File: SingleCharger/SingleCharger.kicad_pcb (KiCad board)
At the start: 2 copper layers, 120 x 130 mm, 77 parts, among them J1 Bus_PCI_Express_x1, J2 Conn_01x03_Pin, J3 Conn_01x02_Pin, J4 Conn_01x02_Pin, Q2 TPHR8504PL,LQ(M1W, U1 ADS1115IDGSR, U10 LM358, U11 MCP4725A0T-E/CH, U2 PICO, U3 TPS54360BDDAR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

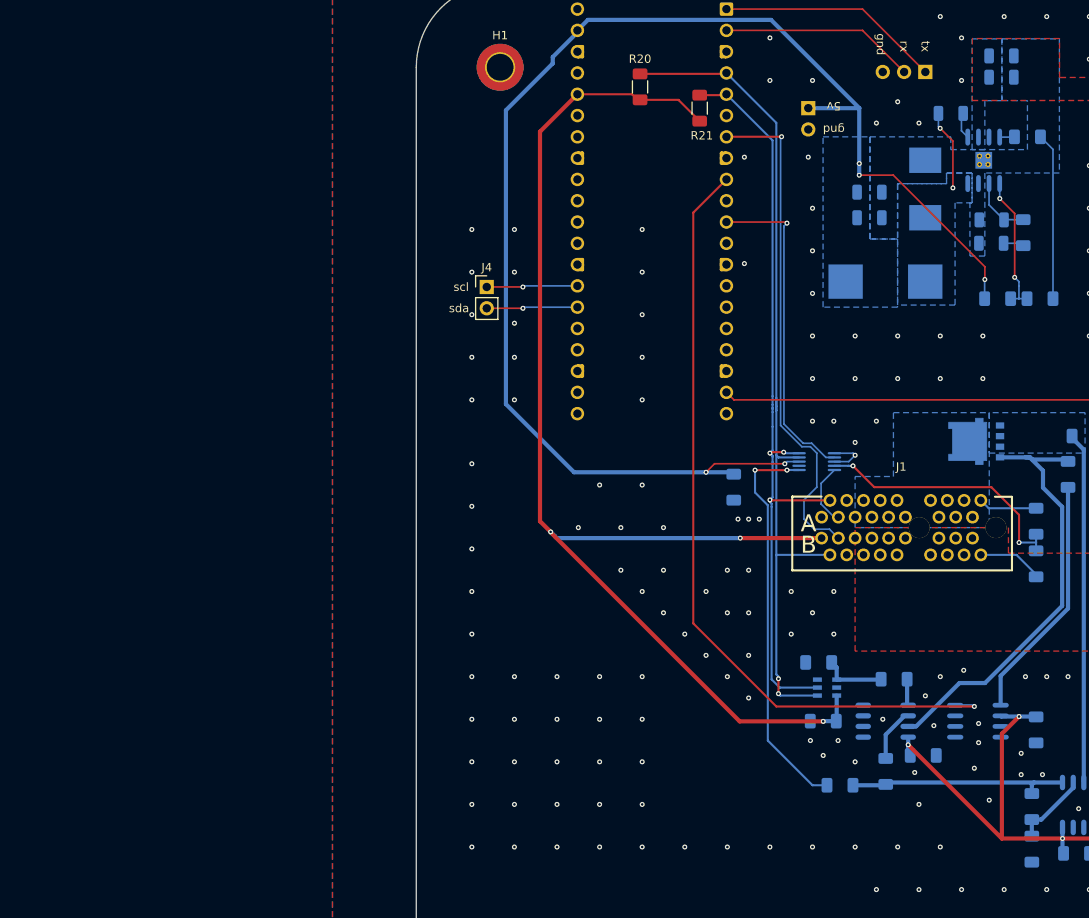
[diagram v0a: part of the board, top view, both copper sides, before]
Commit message: Started adding LEDS
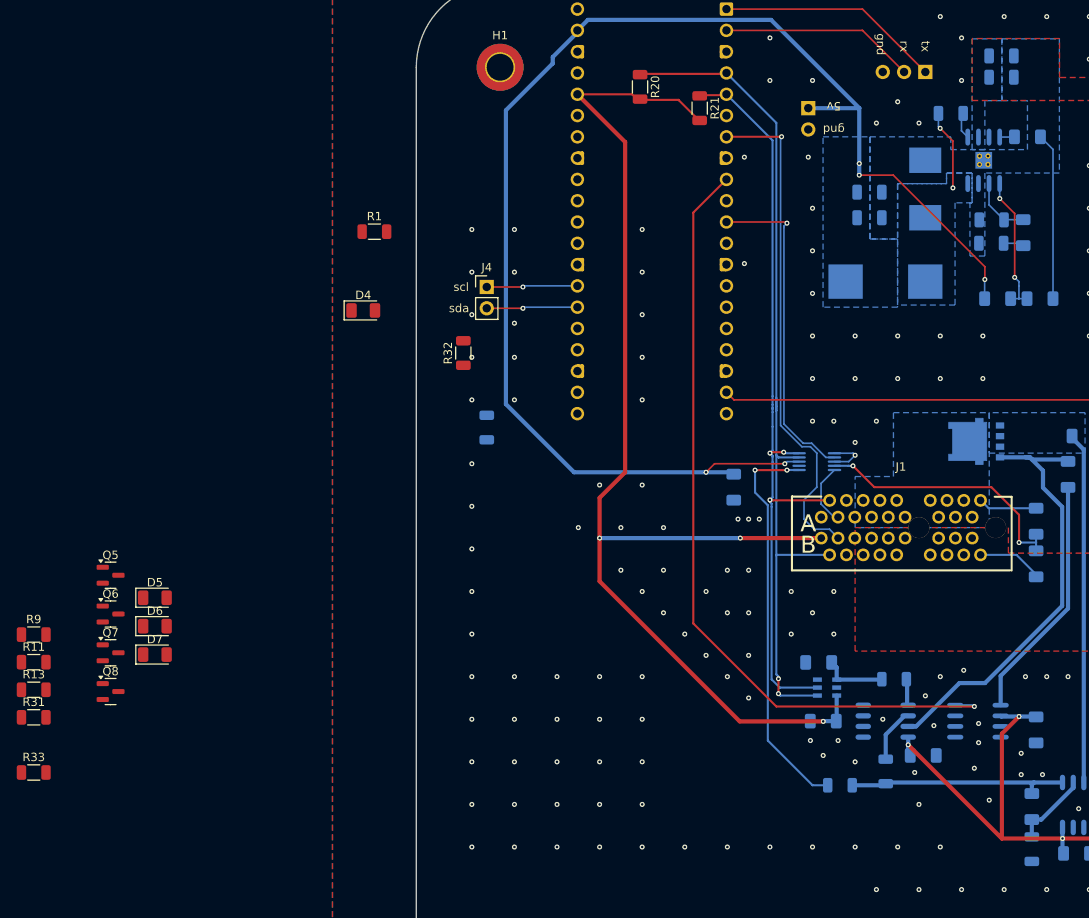
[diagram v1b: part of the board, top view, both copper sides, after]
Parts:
- added D4: LED, LED_SMD:LED_1206_3216Metric, F.Cu at (58.7, 64.0)
- added D5: LED, LED_SMD:LED_1206_3216Metric, F.Cu at (33.8, 98.3)
- added D6: LED, LED_SMD:LED_1206_3216Metric, F.Cu at (33.8, 101.7)
- added D7: LED, LED_SMD:LED_1206_3216Metric, F.Cu at (33.8, 105.1)
- added Q5: NMOS, Package_TO_SOT_SMD:SOT-23, F.Cu at (28.5, 95.6)
- added Q6: NMOS, Package_TO_SOT_SMD:SOT-23, F.Cu at (28.5, 100.2)
- added Q7: NMOS, Package_TO_SOT_SMD:SOT-23, F.Cu at (28.5, 104.8)
- added Q8: NMOS, Package_TO_SOT_SMD:SOT-23, F.Cu at (28.5, 109.5)
- added R1: 1k, Resistor_SMD:R_1206_3216Metric, F.Cu at (60.0, 54.6)
- added R11: 1k, Resistor_SMD:R_1206_3216Metric, F.Cu at (19.4, 106.0)
- added R13: 1k, Resistor_SMD:R_1206_3216Metric, F.Cu at (19.4, 109.3)
- added R31: 1k, Resistor_SMD:R_1206_3216Metric, F.Cu at (19.4, 112.5)
- added R32: 1k, Resistor_SMD:R_1206_3216Metric, F.Cu at (70.6, 69.1)
- added R33: 1k, Resistor_SMD:R_1206_3216Metric, F.Cu at (19.4, 119.1)
- added R5: 1k, Resistor_SMD:R_1206_3216Metric, B.Cu at (73.4, 78.0)
- added R9: 1k, Resistor_SMD:R_1206_3216Metric, F.Cu at (19.4, 102.7)
- R14, R20, R21, R22, R23, R25: footprint Resistor_SMD:R_1206_3216Metric_Pad1.30x1.75mm_HandSolder -> Resistor_SMD:R_1206_3216Metric
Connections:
- U2 pad 21: unconnected-(U2-GP16-Pad21) -> Net-(U2-GP16)
- U2 pad 22: unconnected-(U2-GP17-Pad22) -> Net-(U2-GP17)
- U2 pad 24: unconnected-(U2-GP18-Pad24) -> Net-(U2-GP18)
- U2 pad 25: unconnected-(U2-GP19-Pad25) -> Net-(U2-GP19)
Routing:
- net +3V3: track 149.7 -> 142.4 mm

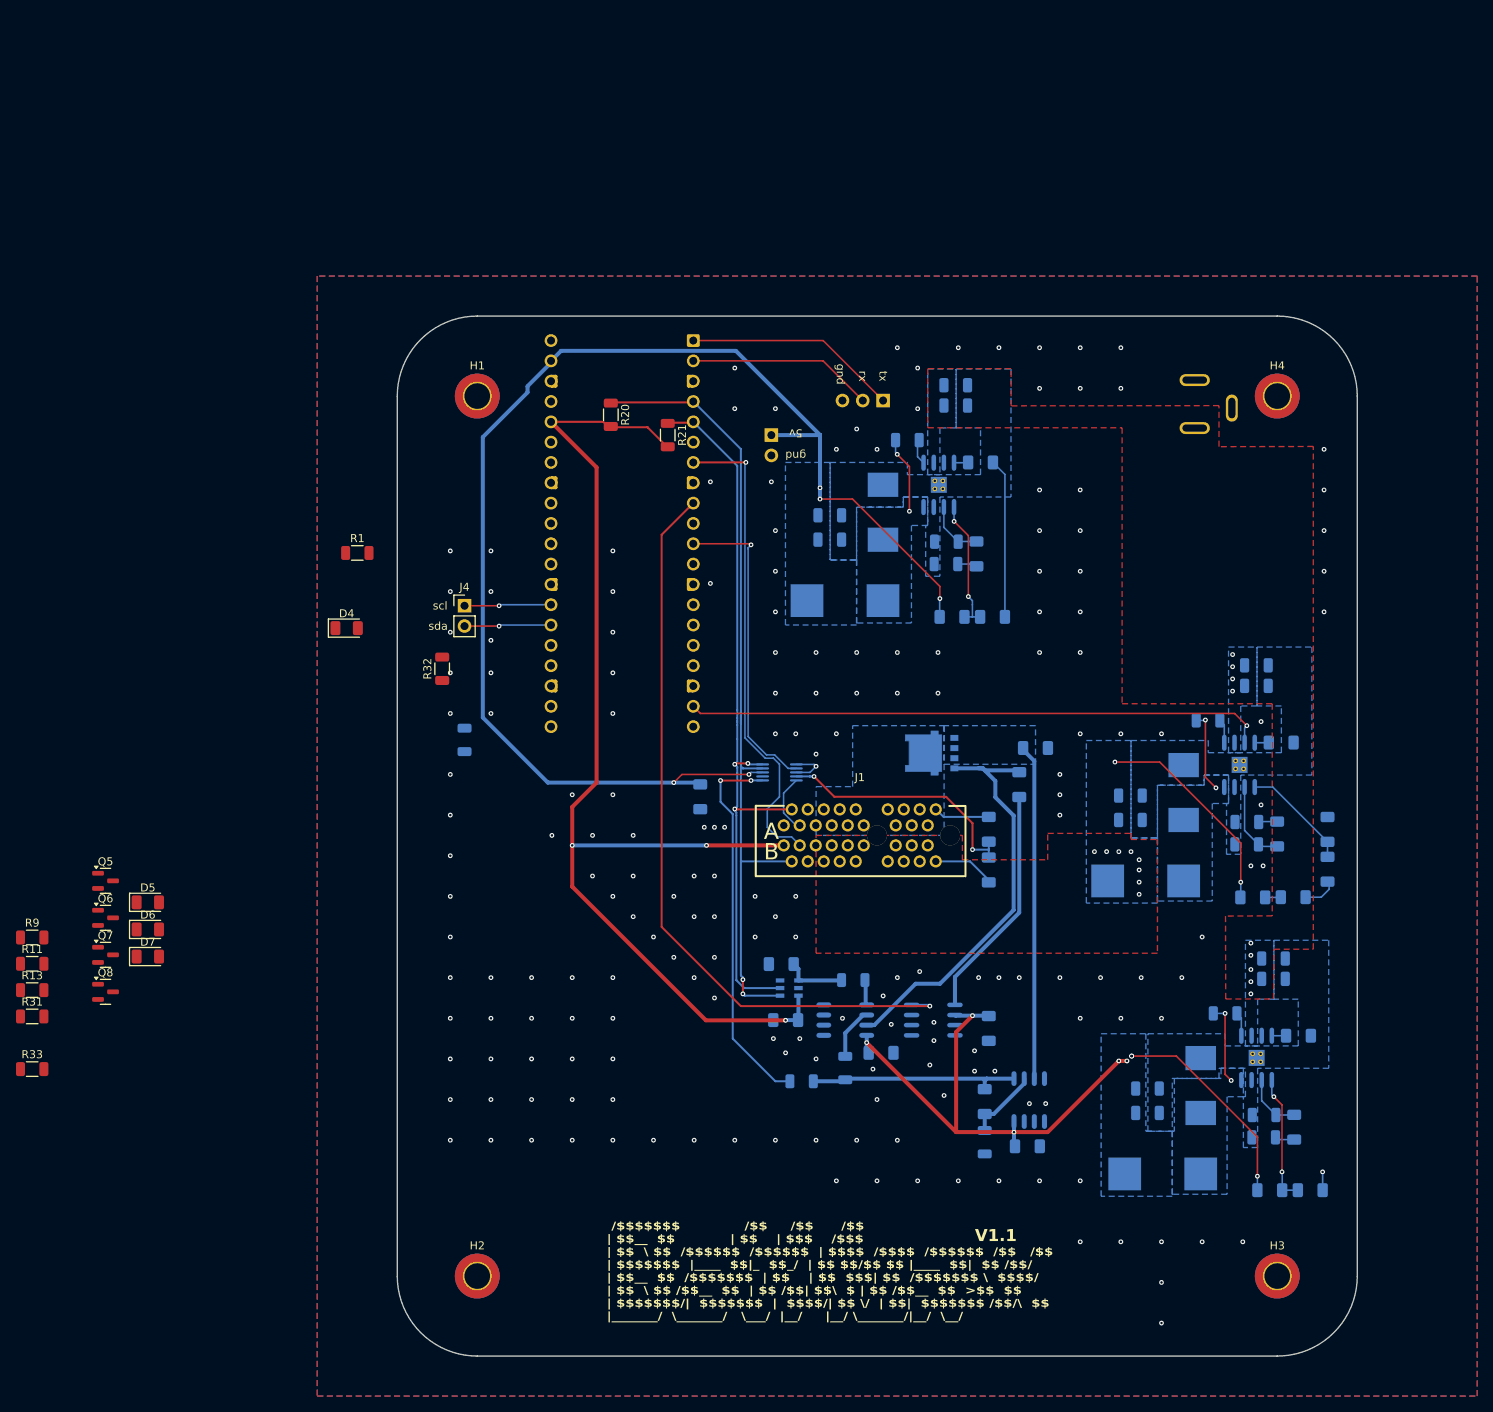
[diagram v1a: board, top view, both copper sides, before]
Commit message: Added LEDS.
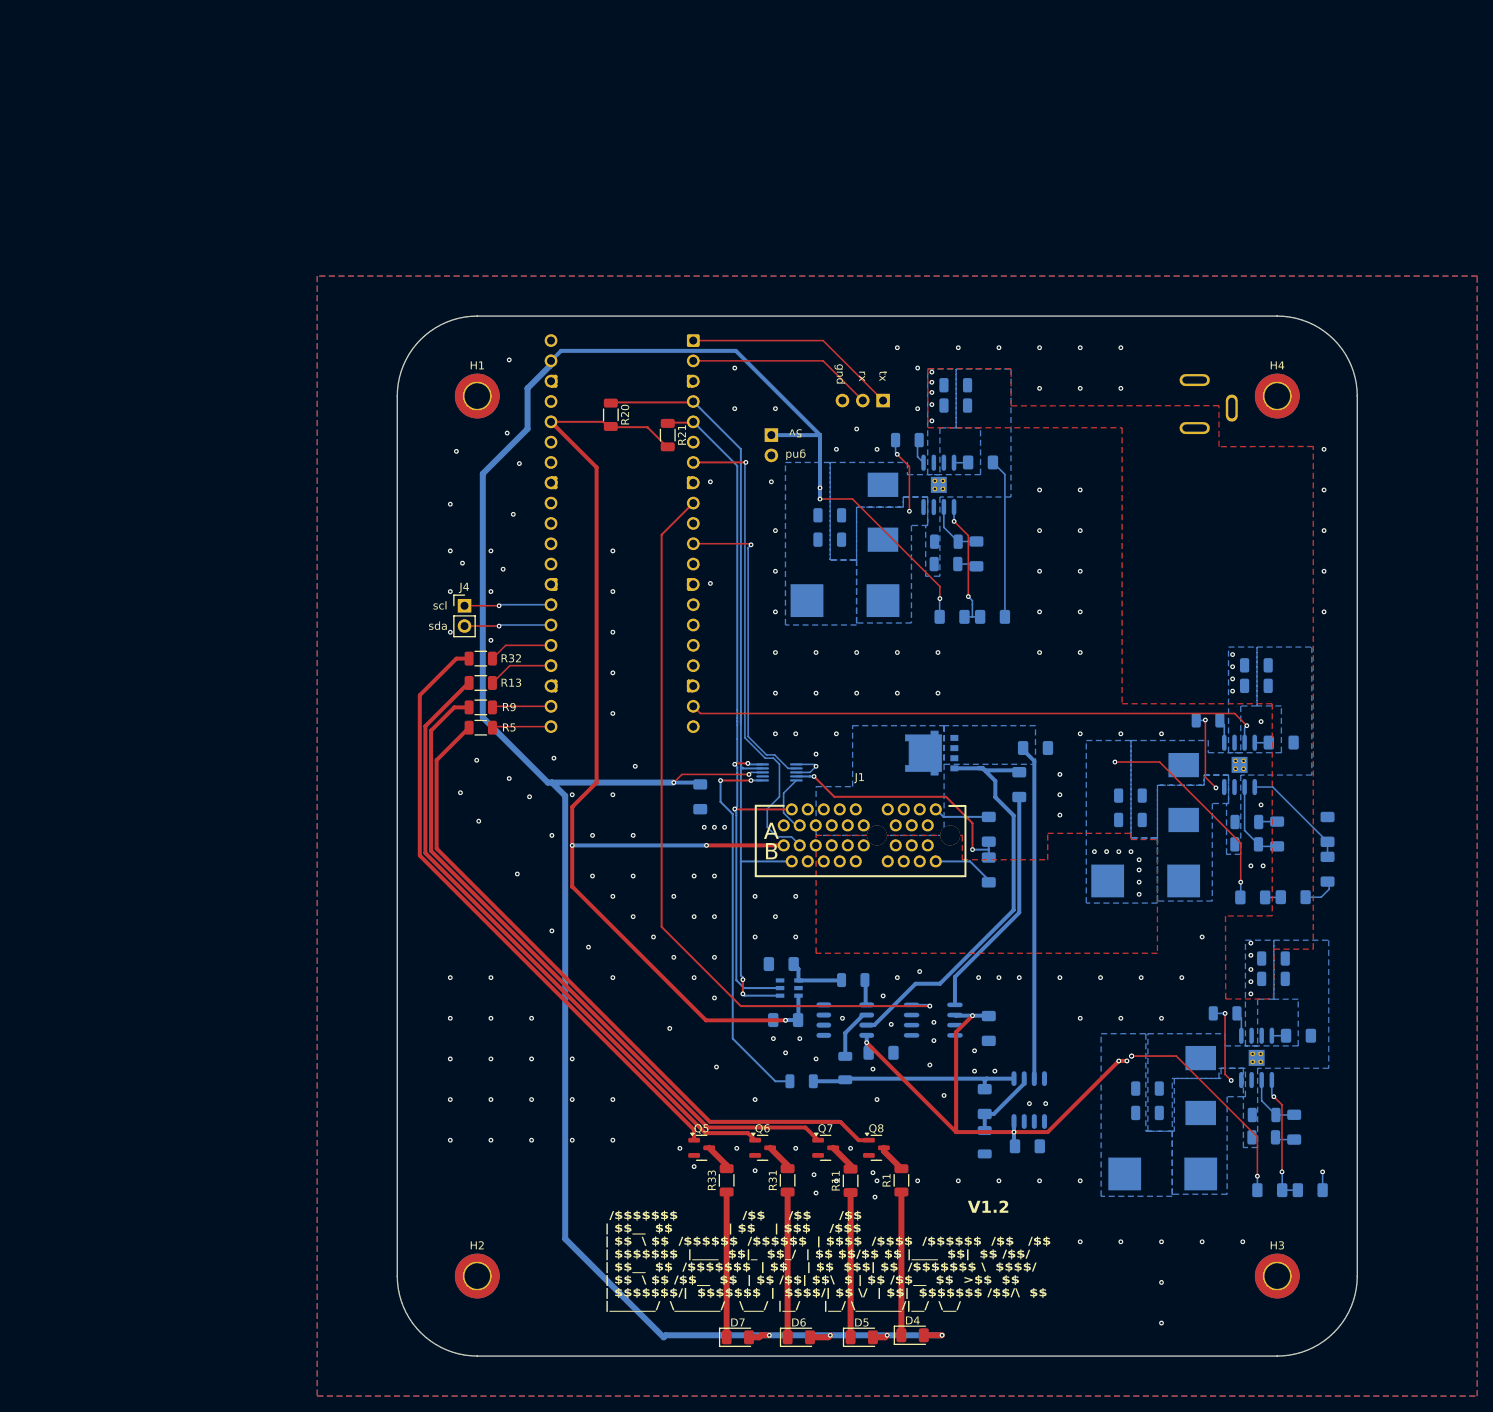
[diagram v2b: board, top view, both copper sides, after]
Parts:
- R5: moved to F.Cu
- moved D4 113.2 mm to (129.4, 152.4)
- moved R11 105.8 mm to (121.7, 133.1), turned to 90 degrees
- moved D5 104.5 mm to (123.1, 152.7)
- moved R1 103.8 mm to (128.0, 133.0), turned to 90 degrees
- moved Q8 98.3 mm to (124.9, 129.0)
- moved R31 96.6 mm to (113.8, 133.0), turned to 90 degrees
- moved D6 96.0 mm to (115.2, 152.7)
- moved Q7 93.2 mm to (118.5, 129.0)
- moved R33 87.9 mm to (106.2, 133.0), turned to 90 degrees
- moved D7 87.8 mm to (107.6, 152.7)
- moved Q6 87.0 mm to (110.7, 129.0)
- moved Q5 81.6 mm to (103.0, 129.0)
- moved R13 68.0 mm to (75.4, 70.9), turned to 180 degrees
- moved R9 63.0 mm to (75.4, 73.9), turned to 180 degrees
- moved R32 4.99 mm to (75.4, 67.8), turned to 180 degrees
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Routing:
- net +5V: track 167.0 -> 286.5 mm, vias 5 -> 9
- net Net-(Q8-G): track 0.00 -> 85.9 mm
- net Net-(Q7-G): track 0.00 -> 84.3 mm
- net Net-(Q6-G): track 0.00 -> 79.6 mm
- net Net-(Q5-G): track 0.00 -> 77.9 mm
- net Net-(D7-K): track 0.00 -> 18.2 mm
- net Net-(D6-K): track 0.00 -> 18.2 mm
- net Net-(D5-K): track 0.00 -> 18.1 mm
- net Net-(D4-K): track 0.00 -> 17.9 mm
- net Net-(U2-GP18): track 0.00 -> 8.22 mm
- net Net-(U2-GP19): track 0.00 -> 8.01 mm
- net Net-(U2-GP17): track 0.00 -> 7.38 mm
- net Net-(U2-GP16): track 0.00 -> 7.38 mm
- net Net-(Q7-D): track 0.00 -> 3.57 mm
- net Net-(Q6-D): track 0.00 -> 3.51 mm
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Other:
- board text added: "V1.2"
- board text removed: "V1.1"

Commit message: Working on fixing PICO.
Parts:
- U2: footprint Module:RaspberryPi_Pico_Common_THT -> Module:RaspberryPi_Pico_SMD
- moved J4 70.4 mm to (76.7, -9.14)
- moved U2 27.3 mm to (94.5, 54.4)
- moved R21 24.8 mm to (97.0, 15.2)
- moved R20 22.5 mm to (91.7, 14.8)
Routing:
- net +5V: track 286.5 -> 212.6 mm, vias 9 -> 10
- net +3V3: track 142.4 -> 74.7 mm
- net /BatteryCC/ChargeLV: track 94.6 -> 40.0 mm
- net /SDA: track 102.5 -> 83.7 mm
- net /SCL: track 92.4 -> 81.4 mm
- net /SDA0: track 10.9 -> 0.00 mm, vias 1 -> 0
- net /SCL0: track 10.9 -> 0.00 mm, vias 1 -> 0
- net /BatteryCC/Battery/EEPROM_WC: track 60.3 -> 53.7 mm
- net Net-(J2-Pin_1): track 26.8 -> 24.2 mm, vias 0 -> 1
- net Net-(U2-GP16): track 7.38 -> 8.74 mm, vias 0 -> 1
- net Net-(U2-GP17): track 7.38 -> 8.74 mm, vias 0 -> 1
- net Net-(J2-Pin_2): track 23.2 -> 22.0 mm, vias 0 -> 1
- net Net-(U2-GP18): track 8.22 -> 7.90 mm, vias 0 -> 1
- net Net-(U2-GP19): track 8.01 -> 8.11 mm, vias 0 -> 1
- net GND: vias 198 -> 135

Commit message: Finished with layout changes.
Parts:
- added J5: Conn_01x03_Pin, Connector_PinHeader_2.54mm:PinHeader_1x03_P2.54mm_Horizontal, F.Cu at (143.5, 35.6)
- J2: footprint Connector_PinHeader_2.54mm:PinHeader_1x03_P2.54mm_Vertical -> Connector_PinHeader_2.54mm:PinHeader_1x03_P2.54mm_Horizontal; moved to F.Cu
- J3: footprint Connector_PinHeader_2.54mm:PinHeader_1x02_P2.54mm_Vertical -> Connector_PinHeader_2.54mm:PinHeader_1x02_P2.54mm_Horizontal; moved to F.Cu
- J4: footprint Connector_PinHeader_2.54mm:PinHeader_1x02_P2.54mm_Vertical -> Connector_PinHeader_2.54mm:PinHeader_1x02_P2.54mm_Horizontal
- moved J4 89.0 mm to (153.7, 35.6), turned to 90 degrees
- moved R20 30.8 mm to (94.0, 45.5)
- moved R21 30.3 mm to (96.8, 45.5)
- moved J2 5.08 mm to (120.7, 35.6)
- moved J3 4.44 mm to (110.7, 35.6), turned to 90 degrees
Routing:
- net /SDA0: track 0.00 -> 98.7 mm, vias 0 -> 2
- net /SCL0: track 0.00 -> 98.5 mm, vias 0 -> 2
- net Net-(J5-Pin_1): track 0.00 -> 96.3 mm, vias 0 -> 2
- net Net-(J5-Pin_3): track 0.00 -> 96.3 mm, vias 0 -> 2
- net Net-(J5-Pin_2): track 0.00 -> 95.2 mm, vias 0 -> 2
- net +5V: track 212.6 -> 286.2 mm, vias 10 -> 9
- net /BatteryCC/ChargeLV: track 40.0 -> 102.5 mm, vias 1 -> 4
- net +3V3: track 74.7 -> 125.5 mm, vias 3 -> 2
- net /SDA: track 83.7 -> 103.6 mm, vias 2 -> 3
- net /SCL: track 81.4 -> 98.4 mm, vias 3 -> 4
- net /BatteryCC/Battery/EEPROM_WC: track 53.7 -> 66.7 mm, vias 1 -> 2
- net /BatteryCC/ALERT/RDY: track 39.1 -> 45.5 mm, vias 1 -> 2
- net Net-(J2-Pin_1): track 24.2 -> 18.7 mm
- net /Power Delivery/EN_BAT_V: track 72.0 -> 77.3 mm, vias 1 -> 2
- net Net-(J2-Pin_2): track 22.0 -> 20.2 mm, vias 1 -> 0
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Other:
- board text added: "LM393"
